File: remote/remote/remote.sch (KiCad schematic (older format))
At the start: 14 parts

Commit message: add new keycad connection for the remote
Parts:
- removed SW_on: SW_SPDT, symbol Switch:SW_SPDT
- added BZ?: Buzzer, symbol Device:Buzzer
- added R1, R2: 4k7, symbol Device:R
- added R3: 100k, symbol Device:R
- added R4: 33k, symbol Device:R
- added SWon: SW_DPDT_x2, symbol Switch:SW_DPDT_x2
- U?: symbol remote:LCD1602_I2c -> remote-rescue:LCD1602_I2c-remote
- U?: symbol remote:cc2500 -> remote-rescue:cc2500-remote
- U?: symbol remote:stm32 -> remote-rescue:stm32-remote
- U?: symbol remote:LI_Charger -> remote-rescue:LI_Charger-remote
- left, right: symbol remote:joystick -> remote-rescue:joystick-remote
- gave numbers to parts that had none: 4
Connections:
- net +3V3: now also BZ?.1 (-), R1.2, R2.2
- net +5V: now also SWon.2 (B); no longer U?.~ (Vout)
- net sda: now reaches U?.~ (VCC)
- net sda: now also U?.~ (VBAT), R2.1
- net usb_5v: now reaches U?.~ (VBAT)
- net usb_5v: now also SWon.3 (C), SWon.4 (A); no longer U?.~ (VCC)
- net sw_mode: now reaches SW_mode.2 (B), U?.~ (VBAT)
- net sw_prearm: now reaches SW_prearm.2 (B), U?.~ (VBAT)
- net sw_beep: now reaches SW_beep.2 (B), U?.~ (VBAT)
- net sw_led: now reaches SW_led.2 (B), U?.~ (VBAT)
- net sw_stickmenu: now reaches SW_stickmenu.2 (B), U?.~ (VBAT)
- net sw_arm: now reaches SW_arm.2 (B), U?.~ (VBAT)
- net at BT?.2 (-), U?.~ (Vout): now also R3.1
- net at BT?.1 (+): now also U?.~ (Vout), R4.2
- new net: U?.~ (VBAT), U?.~ (VCC) (x4)
- new net: U?.~ (VBAT), left.~ (Y) (x2)
- new net: U?.~ (VBAT), right.~ (Y) (x3)
- new net: BZ?.2 (+), U?.~ (VBAT)
- new net: SWon.1 (A), U?.~ (Vout)
- new net: SWon.5 (B), U?.~ (Vout)
- new net Vbat: R3.2, R4.1, U?.~ (VBAT)
- new net scl: R1.1, U?.~ (VBAT), U?.~ (VCC)
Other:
- moved on the sheet: BT?, SW_arm, SW_beep, SW_led, SW_prearm, SW_stickmenu, U?, left, right

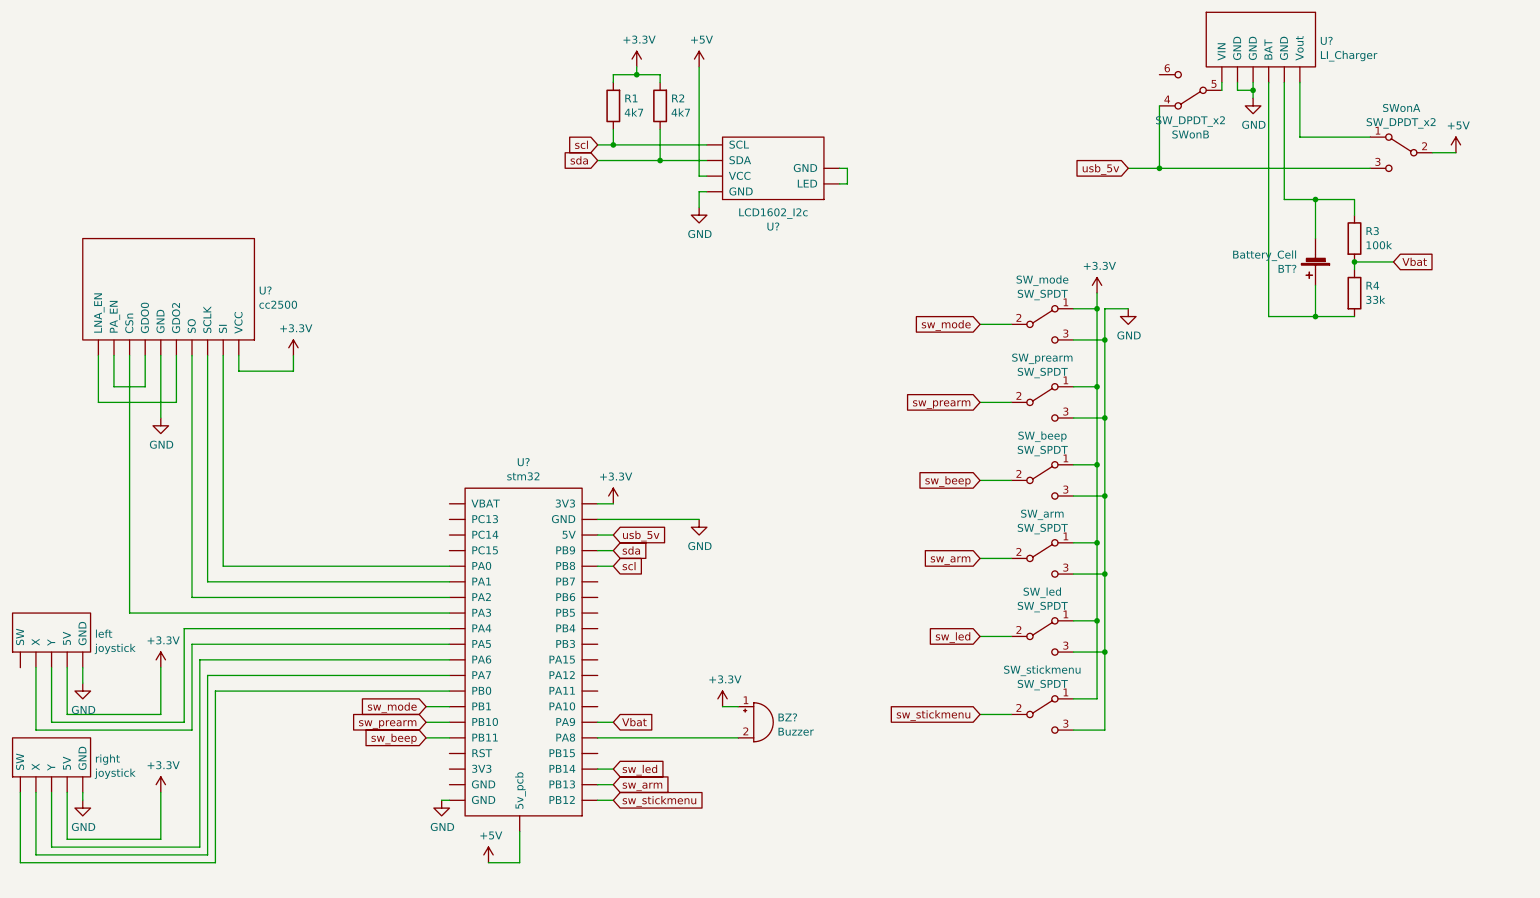
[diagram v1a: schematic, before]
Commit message: add bootloader add eschema pdf and add optinal usb
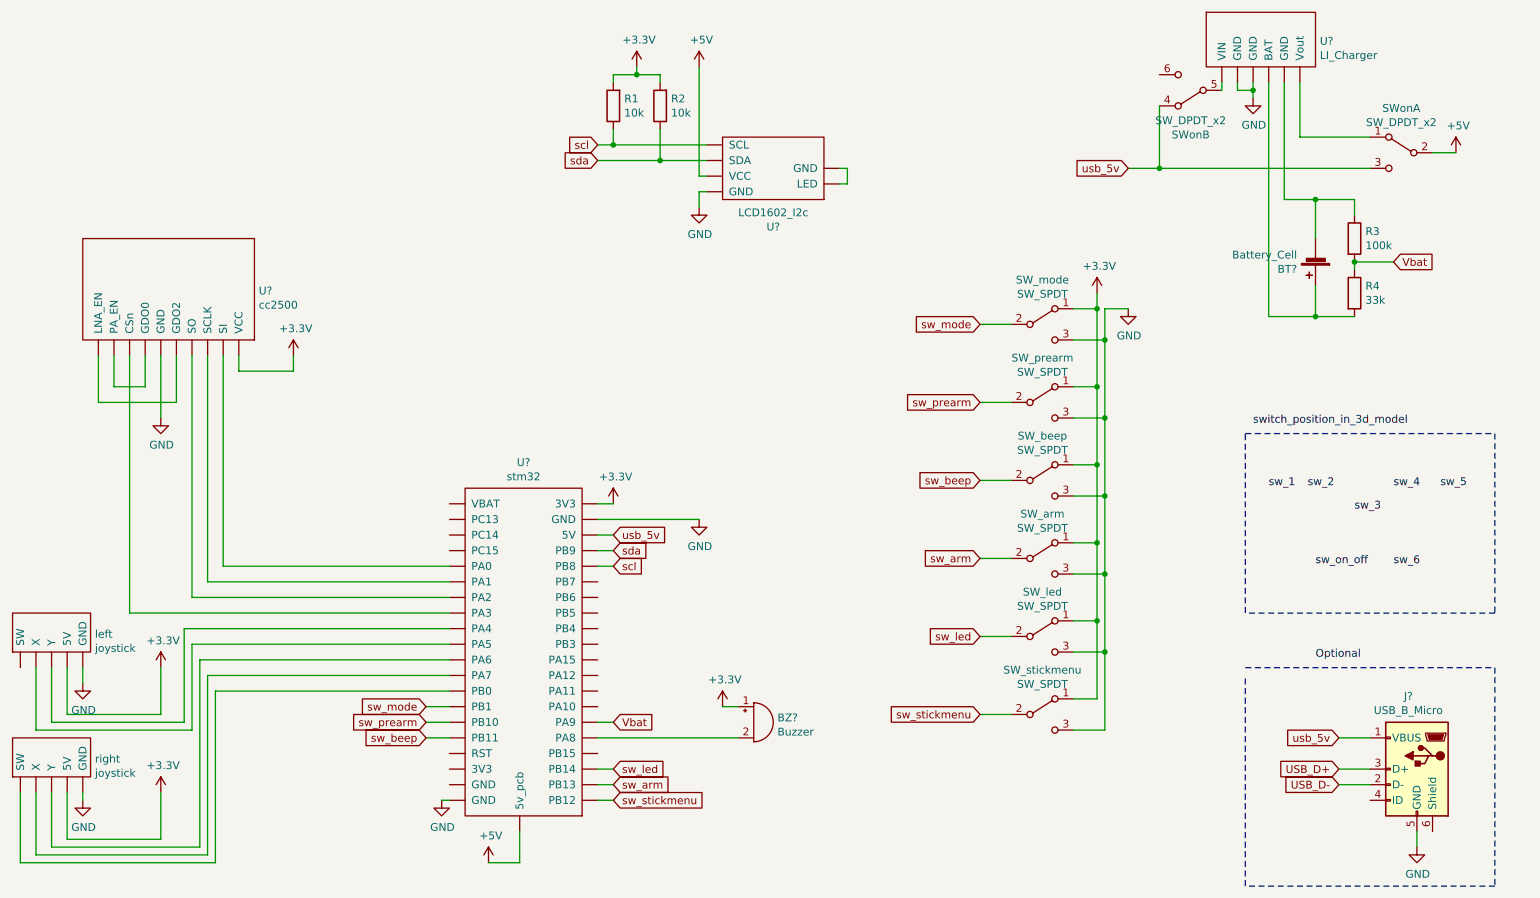
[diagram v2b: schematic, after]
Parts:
- added J?: USB_B_Micro, symbol Connector:USB_B_Micro
- R1, R2: value 4k7 -> 10k
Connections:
- net GND: now also J?.5 (GND)
- net usb_5v: now also J?.1 (VBUS)
- new net: U?.~ (VBAT), U?.~ (VCC) (x4)
- new net: U?.~ (VBAT), left.~ (Y) (x2)
- new net: U?.~ (VBAT), right.~ (Y) (x3)
- new net USB_D+: J?.3 (D+)
- new net USB_D-: J?.2 (D-)
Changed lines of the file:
@@
 EESchema Schematic File Version 4
 LIBS:remote-cache
-EELAYER 29 0
+EELAYER 26 0
 EELAYER END
 $Descr A4 11693 8268
@@
 P 5300 1250
 F 0 "R1" H 5230 1204 50  0000 R CNN
-F 1 "4k7" H 5230 1295 50  0000 R CNN
+F 1 "10k" H 5230 1295 50  0000 R CNN
 F 2 "" V 5230 1250 50  0001 C CNN
 F 3 "~" H 5300 1250 50  0001 C CNN
@@
 P 5600 1250
 F 0 "R2" H 5530 1204 50  0000 R CNN
-F 1 "4k7" H 5530 1295 50  0000 R CNN
+F 1 "10k" H 5530 1295 50  0000 R CNN
 F 2 "" V 5530 1250 50  0001 C CNN
 F 3 "~" H 5600 1250 50  0001 C CNN
@@
 	8800 1650 10150 1650
 Connection ~ 8800 1650
+$Comp
+L Connector:USB_B_Micro J?
+U 1 1 5C8B0CE8
+P 10450 5500
+F 0 "J?" H 10505 5967 50  0000 C CNN
+F 1 "USB_B_Micro" H 10505 5876 50  0000 C CNN
+F 2 "" H 10600 5450 50  0001 C CNN
+F 3 "~" H 10600 5450 50  0001 C CNN
+	1    10450 5500
+	-1   0    0    -1
+$EndComp
+Text GLabel 9950 5500 0    50   Input ~ 0
+USB_D+
+Text GLabel 9950 5600 0    50   Input ~ 0
+USB_D-
+Wire Wire Line
+	9950 5500 10150 5500
+Wire Wire Line
+	10150 5600 9950 5600
+Text GLabel 9950 5300 0    50   Input ~ 0
+usb_5v
+Wire Wire Line
+	9950 5300 10150 5300
+$Comp
+L power:GND #PWR?
+U 1 1 5C8C5D83
+P 10450 6000
+F 0 "#PWR?" H 10450 5750 50  0001 C CNN
+F 1 "GND" H 10455 5827 50  0000 C CNN
+F 2 "" H 10450 6000 50  0001 C CNN
+F 3 "" H 10450 6000 50  0001 C CNN
+	1    10450 6000
+	1    0    0    -1
+$EndComp
+Wire Wire Line
+	10450 5900 10450 6000
+Wire Notes Line
+	9350 4850 10950 4850
+Wire Notes Line
+	10950 4850 10950 6250
+Wire Notes Line
+	10950 6250 9350 6250
+Wire Notes Line
+	9350 6250 9350 4900
+Text Label 9800 4800 0    50   ~ 0
+Optional
+Wire Notes Line
+	10950 4500 9350 4500
+Wire Notes Line
+	9350 4500 9350 3350
+Wire Notes Line
+	9350 3350 10950 3350
+Wire Notes Line
+	10950 3350 10950 4500
+Text Label 9500 3700 0    50   ~ 0
+sw_1
+Text Label 9750 3700 0    50   ~ 0
+sw_2
+Text Label 10050 3850 0    50   ~ 0
+sw_3
+Text Label 10300 3700 0    50   ~ 0
+sw_4
+Text Label 10600 3700 0    50   ~ 0
+sw_5
+Text Label 9800 4200 0    50   ~ 0
+sw_on_off
+Text Label 10300 4200 0    50   ~ 0
+sw_6
+Text Label 9400 3300 0    50   ~ 0
+switch_position_in_3d_model
 $EndSCHEMATC

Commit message: update eschema
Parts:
- gave numbers to parts that had none: 7
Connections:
- net USB_D+: now also U1.~ (VBAT)
- net USB_D-: now also U1.~ (VBAT)
- net sw_1: now also SW_mode.2 (B), U1.~ (VBAT)
- net sw_2: now also SW_prearm.2 (B), U1.~ (VBAT)
- net sw_3: now also SW_beep.2 (B), U1.~ (VBAT)
- net sw_4: now also SW_arm.2 (B), U1.~ (VBAT)
- net sw_5: now also SW_led.2 (B), U1.~ (VBAT)
- removed net sw_arm: SW_arm.2 (B), U1.~ (VBAT)
- removed net sw_beep: SW_beep.2 (B), U1.~ (VBAT)
- removed net sw_led: SW_led.2 (B), U1.~ (VBAT)
- removed net sw_mode: SW_mode.2 (B), U1.~ (VBAT)
- removed net sw_prearm: SW_prearm.2 (B), U1.~ (VBAT)
- new net: U1.~ (VBAT), U2.~ (VCC) (x4)
- new net: U1.~ (VBAT), left.~ (Y) (x2)
- new net: U1.~ (VBAT), right.~ (Y) (x3)
- new net charger_watchdog: U1.~ (VBAT)
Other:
- moved on the sheet: J1
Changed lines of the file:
@@
 $EndDescr
 $Comp
-L remote-rescue:cc2500-remote U?
+L remote-rescue:cc2500-remote U2
 U 1 1 5C490843
 P 2450 2450
-F 0 "U?" H 3028 2465 50  0000 L CNN
+F 0 "U2" H 3028 2465 50  0000 L CNN
 F 1 "cc2500" H 3028 2374 50  0000 L CNN
 F 2 "" H 2750 2700 50  0001 C CNN
@@
 $EndComp
 $Comp
-L Device:Battery_Cell BT?
+L Device:Battery_Cell BT1
 U 1 1 5C5FC330
 P 9800 2200
-F 0 "BT?" H 9918 2296 50  0000 L CNN
+F 0 "BT1" H 9918 2296 50  0000 L CNN
 F 1 "Battery_Cell" H 9918 2205 50  0000 L CNN
 F 2 "" V 9800 2260 50  0001 C CNN
@@
 L power:GND #PWR?
 U 1 1 5C7178B9
-P 4200 5700
-F 0 "#PWR?" H 4200 5450 50  0001 C CNN
-F 1 "GND" H 4205 5527 50  0000 C CNN
-F 2 "" H 4200 5700 50  0001 C CNN
-F 3 "" H 4200 5700 50  0001 C CNN
-	1    4200 5700
-	1    0    0    -1
-$EndComp
-Wire Wire Line
-	4200 5700 4250 5700
+P 4050 5700
+F 0 "#PWR?" H 4050 5450 50  0001 C CNN
+F 1 "GND" H 4055 5527 50  0000 C CNN
+F 2 "" H 4050 5700 50  0001 C CNN
+F 3 "" H 4050 5700 50  0001 C CNN
+	1    4050 5700
+	1    0    0    -1
+$EndComp
 Wire Wire Line
 	5200 3800 5300 3800
@@
 Wire Wire Line
 	6800 1650 6750 1650
-Text GLabel 5300 4100 2    50   Input ~ 0
+Text GLabel 5300 4300 2    50   Input ~ 0
 sda
-Text GLabel 5300 4200 2    50   Input ~ 0
+Text GLabel 5300 4400 2    50   Input ~ 0
 scl
 Wire Wire Line
-	5200 4100 5300 4100
-Wire Wire Line
-	5200 4200 5300 4200
+	5200 4300 5300 4300
+Wire Wire Line
+	5200 4400 5300 4400
 Wire Wire Line
 	9300 1100 9300 1150
@@
 	9400 1150 9400 1100
 $Comp
-L remote-rescue:LI_Charger-remote U?
+L remote-rescue:LI_Charger-remote U4
 U 1 1 5C4FB0A2
 P 9450 800
-F 0 "U?" H 9828 765 50  0000 L CNN
+F 0 "U4" H 9828 765 50  0000 L CNN
 F 1 "LI_Charger" H 9828 674 50  0000 L CNN
 F 2 "" H 9700 1000 50  0001 C CNN
@@
 	2750 5000 4250 5000
 Text GLabel 4100 5100 0    50   Input ~ 0
-sw_mode
+sw_1
 Wire Wire Line
 	4250 5100 4100 5100
 Text GLabel 4100 5200 0    50   Input ~ 0
-sw_prearm
+sw_2
 Text GLabel 4100 5300 0    50   Input ~ 0
-sw_beep
+sw_3
 Wire Wire Line
 	4100 5200 4250 5200
@@
 	4250 5300 4100 5300
 Text GLabel 5300 5500 2    50   Input ~ 0
-sw_led
+sw_5
 Text GLabel 5300 5600 2    50   Input ~ 0
-sw_arm
+sw_4
 Text GLabel 5300 5700 2    50   Input ~ 0
 sw_stickmenu
@@
 $EndComp
 Text GLabel 7650 4650 0    50   Input ~ 0
-sw_led
+sw_5
 Text GLabel 7650 4150 0    50   Input ~ 0
-sw_arm
+sw_4
 Text GLabel 7650 5150 0    50   Input ~ 0
 sw_stickmenu
@@
 Connection ~ 8450 4750
 $Comp
-L Device:Buzzer BZ?
+L Device:Buzzer BZ1
 U 1 1 5C9F50A9
 P 6200 5200
-F 0 "BZ?" H 6352 5229 50  0000 L CNN
+F 0 "BZ1" H 6352 5229 50  0000 L CNN
 F 1 "Buzzer" H 6352 5138 50  0000 L CNN
 F 2 "" V 6175 5300 50  0001 C CNN
@@
 	7850 3650 7650 3650
 Text GLabel 7650 3650 0    50   Input ~ 0
-sw_beep
+sw_3
 Wire Wire Line
 	8450 3750 8250 3750
@@
 	8400 2550 8250 2550
 Text GLabel 7650 3150 0    50   Input ~ 0
-sw_prearm
+sw_2
 Wire Wire Line
 	7850 2650 7650 2650
 Text GLabel 7650 2650 0    50   Input ~ 0
-sw_mode
+sw_1
 $Comp
 L Switch:SW_SPDT SW_mode
@@
 	6750 1750 6800 1750
 $Comp
-L remote-rescue:LCD1602_I2c-remote U?
+L remote-rescue:LCD1602_I2c-remote U3
 U 1 1 5C4907C9
 P 6350 1650
-F 0 "U?" H 6375 2025 50  0000 C CNN
+F 0 "U3" H 6375 2025 50  0000 C CNN
 F 1 "LCD1602_I2c" H 6375 1934 50  0000 C CNN
 F 2 "" H 6400 1400 50  0001 C CNN
@@
 $EndComp
 $Comp
-L remote-rescue:stm32-remote U?
+L remote-rescue:stm32-remote U1
 U 1 1 5C490878
 P 4650 4750
-F 0 "U?" H 4725 5965 50  0000 C CNN
+F 0 "U1" H 4725 5965 50  0000 C CNN
 F 1 "stm32" H 4725 5874 50  0000 C CNN
 F 2 "" H 5050 3650 50  0001 C CNN
@@
 Connection ~ 8800 1650
 $Comp
-L Connector:USB_B_Micro J?
+L Connector:USB_B_Micro J1
 U 1 1 5C8B0CE8
-P 10450 5500
-F 0 "J?" H 10505 5967 50  0000 C CNN
-F 1 "USB_B_Micro" H 10505 5876 50  0000 C CNN
-F 2 "" H 10600 5450 50  0001 C CNN
-F 3 "~" H 10600 5450 50  0001 C CNN
-	1    10450 5500
+P 10350 5500
+F 0 "J1" H 10121 5491 50  0000 R CNN
+F 1 "USB_B_Micro" H 10121 5400 50  0000 R CNN
+F 2 "" H 10500 5450 50  0001 C CNN
+F 3 "~" H 10500 5450 50  0001 C CNN
+	1    10350 5500
 	-1   0    0    -1
 $EndComp
-Text GLabel 9950 5500 0    50   Input ~ 0
+Text GLabel 9850 5500 0    50   Input ~ 0
 USB_D+
-Text GLabel 9950 5600 0    50   Input ~ 0
+Text GLabel 9850 5600 0    50   Input ~ 0
 USB_D-
 Wire Wire Line
-	9950 5500 10150 5500
-Wire Wire Line
-	10150 5600 9950 5600
-Text GLabel 9950 5300 0    50   Input ~ 0
+	9850 5500 10050 5500
+Wire Wire Line
+	10050 5600 9850 5600
+Text GLabel 9850 5300 0    50   Input ~ 0
 usb_5v
 Wire Wire Line
-	9950 5300 10150 5300
+	9850 5300 10050 5300
 $Comp
 L power:GND #PWR?
 U 1 1 5C8C5D83
-P 10450 6000
-F 0 "#PWR?" H 10450 5750 50  0001 C CNN
-F 1 "GND" H 10455 5827 50  0000 C CNN
-F 2 "" H 10450 6000 50  0001 C CNN
-F 3 "" H 10450 6000 50  0001 C CNN
-	1    10450 6000
-	1    0    0    -1
-$EndComp
-Wire Wire Line
-	10450 5900 10450 6000
-Wire Notes Line
-	9350 4850 10950 4850
-Wire Notes Line
-	10950 4850 10950 6250
-Wire Notes Line
-	10950 6250 9350 6250
+P 10350 6000
+F 0 "#PWR?" H 10350 5750 50  0001 C CNN
+F 1 "GND" H 10355 5827 50  0000 C CNN
+F 2 "" H 10350 6000 50  0001 C CNN
+F 3 "" H 10350 6000 50  0001 C CNN
+	1    10350 6000
+	1    0    0    -1
+$EndComp
+Wire Wire Line
+	10350 5900 10350 6000
 Wire Notes Line
 	9350 6250 9350 4900
-Text Label 9800 4800 0    50   ~ 0
+Text Label 9400 4800 0    50   ~ 0
 Optional
-Wire Notes Line
-	10950 4500 9350 4500
 Wire Notes Line
 	9350 4500 9350 3350
 Wire Notes Line
-	9350 3350 10950 3350
-Wire Notes Line
-	10950 3350 10950 4500
-Text Label 9500 3700 0    50   ~ 0
+	11100 3350 11100 4500
+Text Label 9450 3700 0    50   ~ 0
 sw_1
-Text Label 9750 3700 0    50   ~ 0
+Text Label 9700 3700 0    50   ~ 0
 sw_2
-Text Label 10050 3850 0    50   ~ 0
+Text Label 10000 3850 0    50   ~ 0
 sw_3
-Text Label 10300 3700 0    50   ~ 0
+Text Label 10250 3700 0    50   ~ 0
 sw_4
-Text Label 10600 3700 0    50   ~ 0
-sw_5
-Text Label 9800 4200 0    50   ~ 0
-sw_on_off
-Text Label 10300 4200 0    50   ~ 0
+Text Label 10550 3700 0    50   ~ 0
+sw_stickmenu
+Text Label 9750 4200 0    50   ~ 0
+sw_on
+Text Label 10250 4200 0    50   ~ 0
 sw_6
 Text Label 9400 3300 0    50   ~ 0
 switch_position_in_3d_model
+Text GLabel 5400 4900 2    50   Input ~ 0
+USB_D-
+Text GLabel 5400 5000 2    50   Input ~ 0
+USB_D+
+Wire Wire Line
+	5400 4900 5200 4900
+Wire Wire Line
+	5200 5000 5400 5000
+Wire Notes Line
+	9350 3350 11100 3350
+Wire Notes Line
+	9350 4500 11100 4500
+Wire Wire Line
+	4250 5600 4050 5600
+Wire Wire Line
+	4050 5600 4050 5700
+Wire Wire Line
+	4050 5700 4250 5700
+Connection ~ 4050 5700
+$Comp
+L power:+3.3V #PWR?
+U 1 1 5C90ECBA
+P 3700 5500
+F 0 "#PWR?" H 3700 5350 50  0001 C CNN
+F 1 "+3.3V" H 3715 5673 50  0000 C CNN
+F 2 "" H 3700 5500 50  0001 C CNN
+F 3 "" H 3700 5500 50  0001 C CNN
+	1    3700 5500
+	1    0    0    -1
+$EndComp
+Wire Wire Line
+	3700 5500 4250 5500
+Wire Notes Line
+	9350 4850 11100 4850
+Wire Notes Line
+	11100 4850 11100 6250
+Wire Notes Line
+	9350 6250 11100 6250
+Text GLabel 4100 4000 0    50   Input ~ 0
+charger_watchdog
+Wire Wire Line
+	4250 4000 4100 4000
 $EndSCHEMATC
